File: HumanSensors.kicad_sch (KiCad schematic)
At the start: 0 parts

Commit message: Human sensors
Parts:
- added C1: 100n, lcsc_footprints:C5656610_MIC-SMD_6P-L3_5-W2_7-P0_90-BL, symbol Device:C
- added C2: 4,7u, symbol Device:C
- added C3: 100n, symbol Device:C
- added C4: 0,1u, lcsc_footprints:C5656610_MIC-SMD_6P-L3_5-W2_7-P0_90-BL, symbol Device:C
- added R1: 2K, lcsc_footprints:C37897213_SENSOR-TH_HLK-LD6002, symbol Device:R
- added R10: 100K, symbol Device:R
- added R6, R7, R9: 10K, symbol Device:R
- added R8: 10K, lcsc_footprints:C2848306_DFN-4_L1_5-W1_5-P0_8-TL-EP, symbol Device:R
- added U10: HLK-LD6002, lcsc_footprints:C37897213_SENSOR-TH_HLK-LD6002, symbol lcsc_imported:HLK-LD6002
- added U6: SCD40-D-R1, lcsc_footprints:C3037696_LGA-20_L10_1-W10_1-P1_25-TL, symbol lcsc_imported:SCD40-D-R1
- added U7: SHT40-AD1B-R3, lcsc_footprints:C2848306_DFN-4_L1_5-W1_5-P0_8-TL-EP, symbol lcsc_imported:SHT40-AD1B-R3
- added U8: ICS-43434_C5656610, lcsc_footprints:C5656610_MIC-SMD_6P-L3_5-W2_7-P0_90-BL, symbol lcsc_imported:ICS-43434_C5656610
- added U9: AM312, lcsc_footprints:C114881_TO-5-3_L8_2-W8_2, symbol lcsc_imported:AM312
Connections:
- new net: R1.2, U10.3 (P19)
- new net AC_BCLK: U8.4 (SCK)
- new net AC_RCLK: U8.1 (WS)
- new net CO2_SCL: R7.2, U6.9 (SCL)
- new net CO2_SDA: R6.2, U6.10 (SDA)
- new net D_IN: R10.1, U8.6 (SD)
- new net GND: C1.1, C2.1, C3.1, C4.2, R1.1, R10.2, U10.2 (GND), U6.21 (GND), U7.4 (VSS), U7.5 (EP), U8.2 (LR), U8.3 (GND), U9.3 (GND)
- new net PIR_OUT: U9.2 (OUT)
- new net R_RX0: U10.8 (RX0)
- new net R_TX0: U10.7 (TX0)
- new net Temp_SCL: R8.1, U7.2 (SCL)
- new net Temp_SDA: R9.1, U7.1 (SDA)
- new net VDD: C1.2, C2.2, C3.2, C4.1, R6.1, R7.1, R8.2, R9.2, U10.1 (3V3), U6.19 (VDDH), U6.7 (VDD), U7.3 (VDD), U8.5 (VDD), U9.1 (VCC)
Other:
- note added: "Acoustic Sensor"
- note added: "CO2 Sensor"
- note added: "PIR Sensor"
- note added: "Radar Sensor"
- note added: "Temp/humidity Sensor"

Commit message: Rework MCU and Human sensor
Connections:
- net GND: now also U6.20 (GND), U6.6 (GND)
- net U0_CTS: now reaches U10.4 (TX2)
- net U0_RTS: now reaches U10.6 (SCL0)
- net AC_RCLK renamed AC_LRCLK
- net R_TX0 renamed R_TXO
- net VDD renamed 3.3V
- no-connect marks 0 -> 15

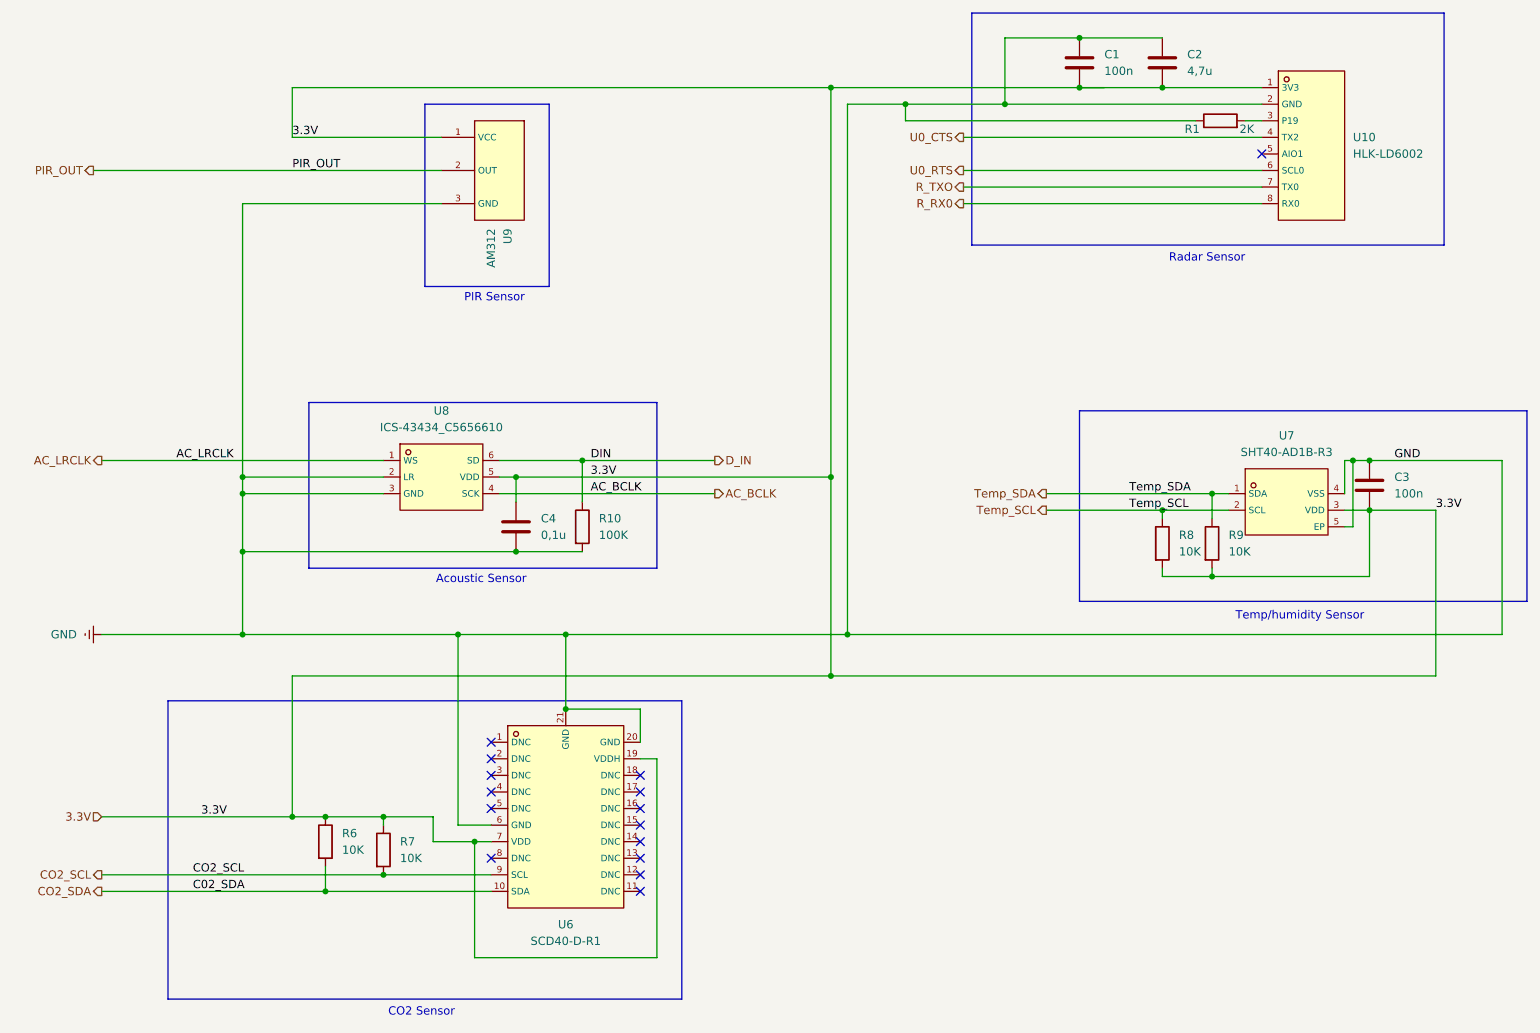
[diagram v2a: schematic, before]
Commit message: Changed the default symbols with JLC's one
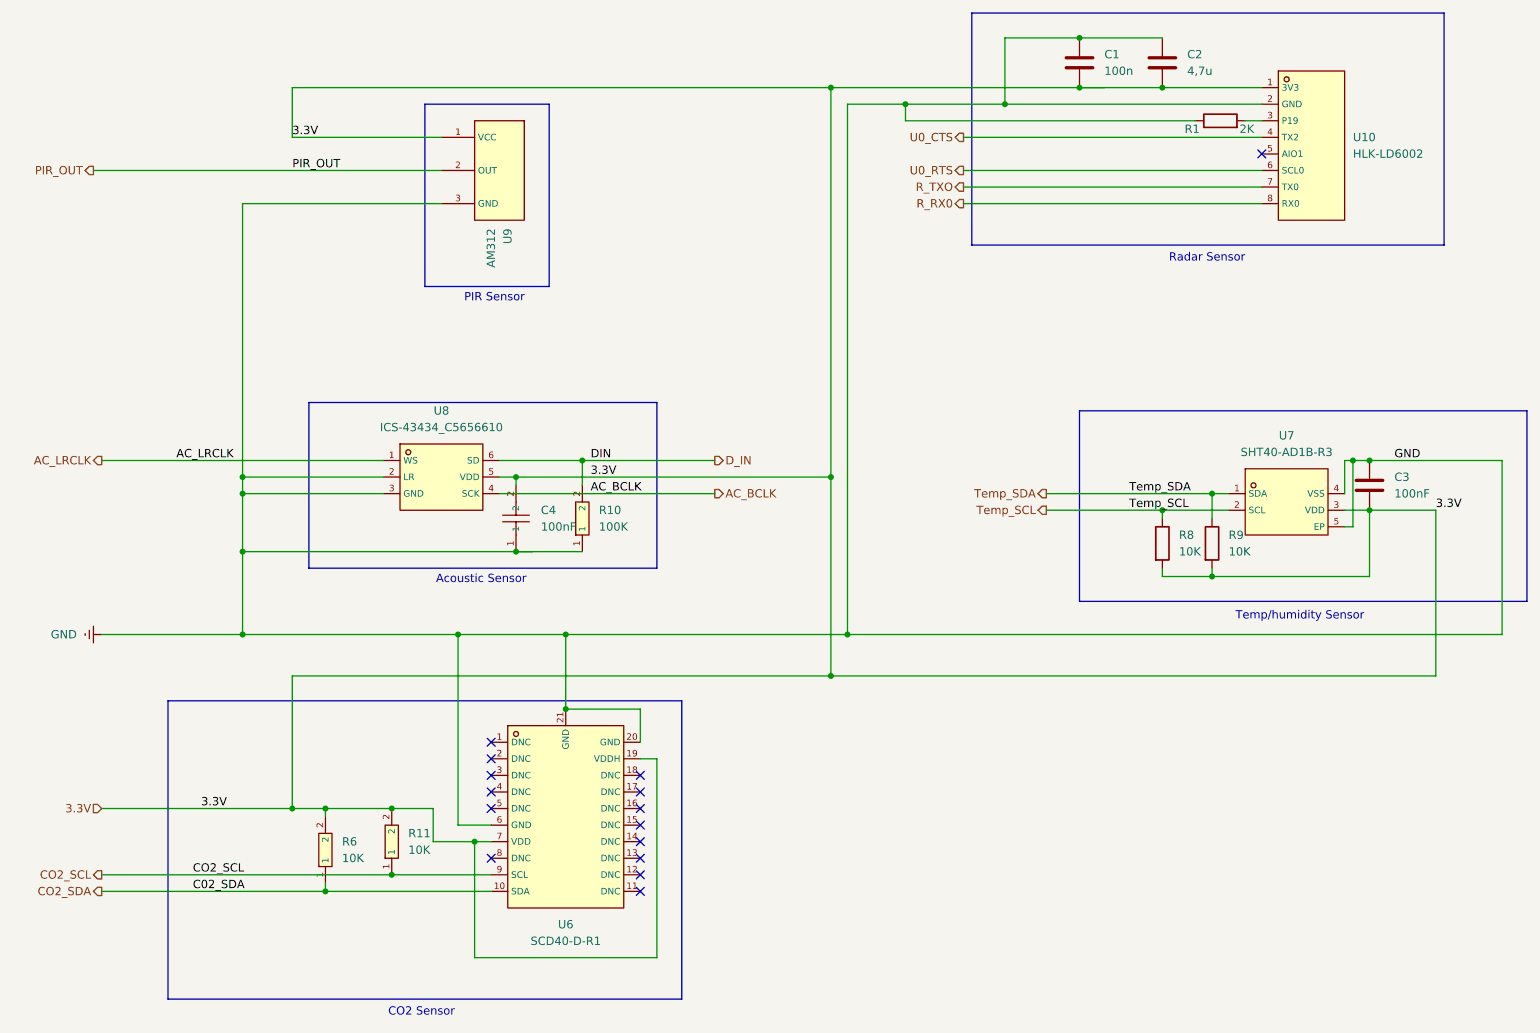
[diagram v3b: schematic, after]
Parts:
- removed R7: 10K, symbol Device:R
- added R11: 10K, lcsc_footprints:C1489_R1206, symbol lcsc_imported:10KΩ_(103)_±5%
- C3: value 100n -> 100nF
- C4: value 0,1u -> 100nF; footprint lcsc_footprints:C5656610_MIC-SMD_6P-L3_5-W2_7-P0_90-BL -> lcsc_footprints:C1525_C0402; symbol Device:C -> lcsc_imported:100nF_(104)_±10%_16V; LCSC (none) -> C1525; Manufacturer (none) -> SAMSUNG(三星)
- R10: footprint (none) -> lcsc_footprints:C14675_R0603; symbol Device:R -> lcsc_imported:RC0603FR-07100KL; LCSC (none) -> C14675; Manufacturer (none) -> YAGEO(国巨)
- R6: footprint (none) -> lcsc_footprints:C1489_R1206; symbol Device:R -> lcsc_imported:10KΩ_(103)_±5%; LCSC (none) -> C1489; Manufacturer (none) -> UNI-ROYAL(厚声)
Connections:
- net 3.3V: now also C4.2, R6.2, R11.2; no longer C4.1, R6.1
- net CO2_SCL: now also R11.1
- net CO2_SDA: now also R6.1; no longer R6.2
- net D_IN: now also R10.2; no longer R10.1
- net GND: now also C4.1, R10.1; no longer C4.2, R10.2

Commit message: Changed footprint of the test point
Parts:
- C15: renamed from C1; value 100n -> 100nF; footprint lcsc_footprints:C5656610_MIC-SMD_6P-L3_5-W2_7-P0_90-BL -> lcsc_footprints:C1525_C0402; symbol Device:C -> lcsc_imported:100nF_(104)_±10%_16V; LCSC (none) -> C1525; Manufacturer (none) -> SAMSUNG(三星)
- C16: renamed from C2; value 4,7u -> 4,7uF; footprint (none) -> lcsc_footprints:C1705_C0603; symbol Device:C -> lcsc_imported:4_7uF_(475)_±10%_10V; LCSC (none) -> C1705; Manufacturer (none) -> SAMSUNG(三星)
- C17: renamed from C3; footprint (none) -> lcsc_footprints:C1525_C0402; symbol Device:C -> lcsc_imported:100nF_(104)_±10%_16V; LCSC (none) -> C1525; Manufacturer (none) -> SAMSUNG(三星)
- R13: renamed from R8; footprint lcsc_footprints:C2848306_DFN-4_L1_5-W1_5-P0_8-TL-EP -> lcsc_footprints:C1489_R1206; symbol Device:R -> lcsc_imported:10KΩ_(103)_±5%; LCSC (none) -> C1489; Manufacturer (none) -> UNI-ROYAL(厚声)
- R14: renamed from R9; footprint (none) -> lcsc_footprints:C1489_R1206; symbol Device:R -> lcsc_imported:10KΩ_(103)_±5%; LCSC (none) -> C1489; Manufacturer (none) -> UNI-ROYAL(厚声)
- R15: renamed from R1; footprint lcsc_footprints:C37897213_SENSOR-TH_HLK-LD6002 -> lcsc_footprints:C4109_R0402; symbol Device:R -> lcsc_imported:2KΩ_(2001)_±1%; LCSC (none) -> C4109; Manufacturer (none) -> UNI-ROYAL(厚声)
- renumbered C4 to C14, R6 to R10, R10 to R12, U8 to U4, U9 to U5, U10 to U8
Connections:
- net 3.3V: now also C15.1, C16.1, C17.1, R13.1, R14.1; no longer C15.2, C16.2, C17.2, R13.2, R14.2
- net GND: now also C15.2, C16.2, C17.2; no longer C15.1, C16.1, C17.1
- net Temp_SCL: now also R13.2; no longer R13.1
- net Temp_SDA: now also R14.2; no longer R14.1

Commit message: KiCad: PCB placement, routing and schematic updates
Wiring of component blocks and sensors + component rearrangement + routing
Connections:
- net R_RX0 renamed U0_RXD
- net R_TXO renamed U0_TXD
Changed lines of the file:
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@@
 		)
 	)
-	(hierarchical_label "R_RX0"
+	(hierarchical_label "U0_RXD"
 		(shape output)
 		(at 163.83 59.69 180)
@@
 		)
 	)
-	(hierarchical_label "R_TXO"
+	(hierarchical_label "U0_TXD"
 		(shape output)
 		(at 163.83 57.15 180)

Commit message: Rerouting
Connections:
- net 3.3V renamed 3V3_SENS
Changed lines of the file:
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@@
 		)
 	)
-	(hierarchical_label "3.3V"
+	(hierarchical_label "3V3_SENS"
 		(shape input)
 		(at 31.75 152.4 180)

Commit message: Fixed som DRC error
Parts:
- C14, C15, C17: LCSC Part (none) -> C1525
- C16: LCSC Part (none) -> C1705
- R10, R11, R13, R14: LCSC Part (none) -> C1489
- R12: LCSC Part (none) -> C14675
- R15: LCSC Part (none) -> C4109
- U4: LCSC Part (none) -> C5656610
- U5: LCSC Part (none) -> C114881
- U6: LCSC Part (none) -> C3037696
- U7: LCSC Part (none) -> C2848306
- U8: LCSC Part (none) -> C37897213
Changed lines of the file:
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@@
+			)
+		)
+		(property "LCSC Part" "C37897213"
+			(at 217.17 50.8 0)
+			(hide yes)
+			(show_name no)
+			(do_not_autoplace no)
+			(effects
+				(font
+					(size 1.27 1.27)
+				)
 			)
 		)
@@
 			)
 		)
+		(property "LCSC Part" "C114881"
+			(at 90.17 54.61 0)
+			(hide yes)
+			(show_name no)
+			(do_not_autoplace no)
+			(effects
+				(font
+					(size 1.27 1.27)
+				)
+			)
+		)
 		(pin "2"
 		)
@@
 			)
 		)
+		(property "LCSC Part" "C1489"
+			(at 66.04 158.75 0)
+			(hide yes)
+			(show_name no)
+			(do_not_autoplace no)
+			(effects
+				(font
+					(size 1.27 1.27)
+				)
+			)
+		)
 		(pin "2"
 		)
@@
 			)
 		)
+		(property "LCSC Part" "C2848306"
+			(at 213.36 105.41 0)
+			(hide yes)
+			(show_name no)
+			(do_not_autoplace no)
+			(effects
+				(font
+					(size 1.27 1.27)
+				)
+			)
+		)
 		(pin "3"
 		)
@@
 			)
 		)
+		(property "LCSC Part" "C1489"
+			(at 194.31 113.03 0)
+			(hide yes)
+			(show_name no)
+			(do_not_autoplace no)
+			(effects
+				(font
+					(size 1.27 1.27)
+				)
+			)
+		)
 		(pin "2"
 		)
@@
 		)
 		(property "Manufacturer" "SAMSUNG(三星)"
+			(at 227.33 101.6 0)
+			(hide yes)
+			(show_name no)
+			(do_not_autoplace no)
+			(effects
+				(font
+					(size 1.27 1.27)
+				)
+			)
+		)
+		(property "LCSC Part" "C1525"
 			(at 227.33 101.6 0)
 			(hide yes)
@@
 			)
 		)
+		(property "LCSC Part" "C1489"
+			(at 76.2 157.48 0)
+			(hide yes)
+			(show_name no)
+			(do_not_autoplace no)
+			(effects
+				(font
+					(size 1.27 1.27)
+				)
+			)
+		)
 		(pin "2"
 		)
@@
 			)
 		)
+		(property "LCSC Part" "C1525"
+			(at 179.07 36.83 0)
+			(hide yes)
+			(show_name no)
+			(do_not_autoplace no)
+			(effects
+				(font
+					(size 1.27 1.27)
+				)
+			)
+		)
 		(pin "1"
 		)
@@
 		)
 		(property "Manufacturer" "UNI-ROYAL(厚声)"
+			(at 201.93 46.99 0)
+			(hide yes)
+			(show_name no)
+			(do_not_autoplace no)
+			(effects
+				(font
+					(size 1.27 1.27)
+				)
+			)
+		)
+		(property "LCSC Part" "C4109"
 			(at 201.93 46.99 0)
 			(hide yes)
@@
 			)
 		)
+		(property "LCSC Part" "C14675"
+			(at 105.41 107.95 0)
+			(hide yes)
+			(show_name no)
+			(do_not_autoplace no)
+			(effects
+				(font
+					(size 1.27 1.27)
+				)
+			)
+		)
 		(pin "2"
 		)
@@
 			)
 		)
+		(property "LCSC Part" "C3037696"
+			(at 102.87 152.4 0)
+			(hide yes)
+			(show_name no)
+			(do_not_autoplace no)
+			(effects
+				(font
+					(size 1.27 1.27)
+				)
+			)
+		)
 		(pin "1"
 		)
@@
 			)
 		)
+		(property "LCSC Part" "C5656610"
+			(at 83.82 101.6 0)
+			(hide yes)
+			(show_name no)
+			(do_not_autoplace no)
+			(effects
+				(font
+					(size 1.27 1.27)
+				)
+			)
+		)
 		(pin "4"
 		)
@@
 			)
 		)
+		(property "LCSC Part" "C1705"
+			(at 194.31 36.83 0)
+			(hide yes)
+			(show_name no)
+			(do_not_autoplace no)
+			(effects
+				(font
+					(size 1.27 1.27)
+				)
+			)
+		)
 		(pin "1"
 		)
@@
 			)
 		)
+		(property "LCSC Part" "C1525"
+			(at 95.25 107.95 0)
+			(hide yes)
+			(show_name no)
+			(do_not_autoplace no)
+			(effects
+				(font
+					(size 1.27 1.27)
+				)
+			)
+		)
 		(pin "2"
 		)
@@
 			(at 201.93 113.03 0)
 			(hide yes)
+			(show_name no)
+			(do_not_autoplace no)
+			(effects
+				(font
+					(size 1.27 1.27)
+				)
+			)
+		)
+		(property "LCSC Part" "C1489"
+			(at 201.93 113.03 0)
+			(hide yes)
